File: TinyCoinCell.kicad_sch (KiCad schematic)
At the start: 35 parts, among them SW1 SW_Push, U1 nRF54L15-QFAA, X1 32MHz, X2 32.768kHz

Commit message: Updated with BOM
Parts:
- BT1: LCSC (none) -> C22417572
- C1, C2, C3, C4: LCSC (none) -> C2903664
- C10, C7: LCSC (none) -> C5377657
- C11, C14: LCSC (none) -> C723329
- C12: LCSC (none) -> C7393836
- C13: LCSC (none) -> C5142540
- C5: LCSC (none) -> C15525
- C6: LCSC (none) -> C18164554
- C8: LCSC (none) -> C18164580
- C9: LCSC (none) -> C18164556
- D1: LCSC (none) -> C52675989
- FB1: LCSC (none) -> C97850
- L1: LCSC (none) -> C295681
- L2: LCSC (none) -> C370148
- L3, L4, L5: LCSC (none) -> C52109755
- R1: LCSC (none) -> C102683
- R2: LCSC (none) -> C4125
- SW1: LCSC (none) -> C139797
- U1: LCSC (none) -> C42458750
- X1: LCSC (none) -> C2965582
- X2: LCSC (none) -> C2838163

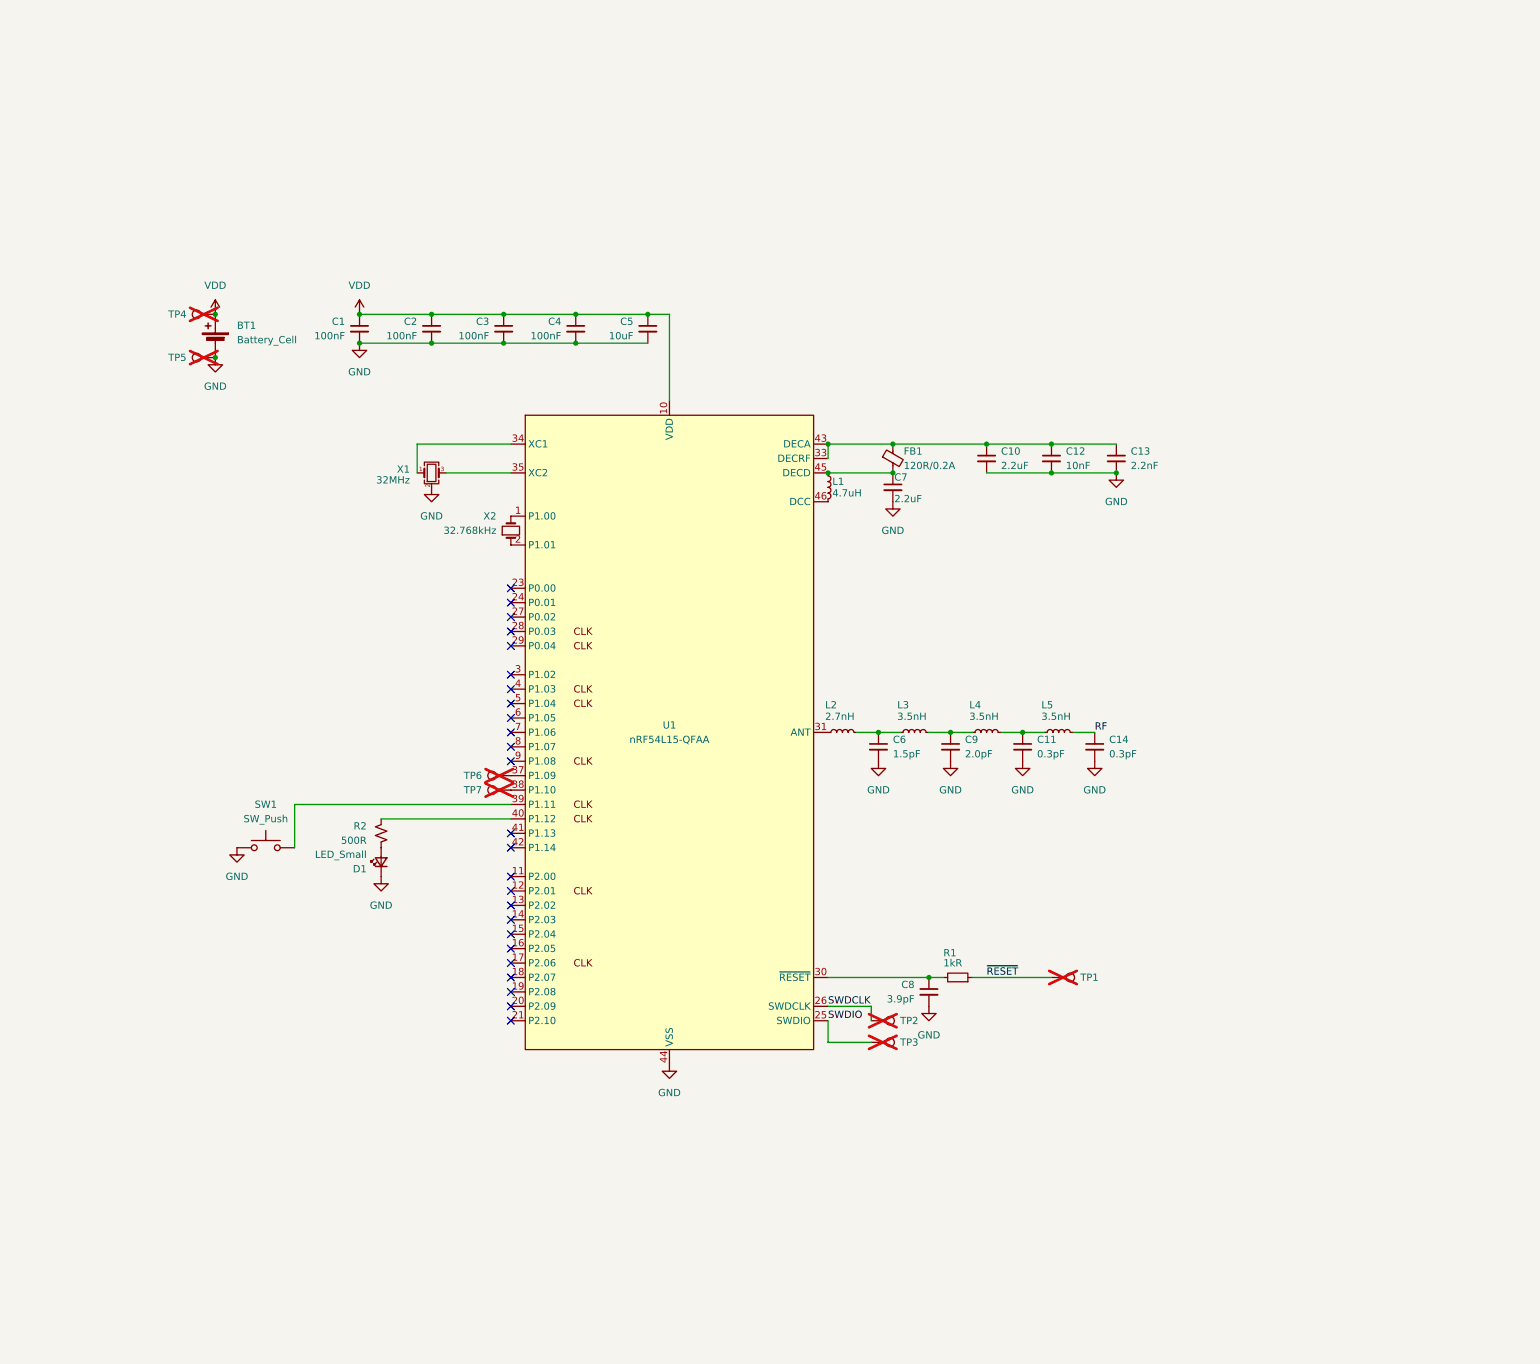
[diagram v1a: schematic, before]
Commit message: Updates for nPM2100
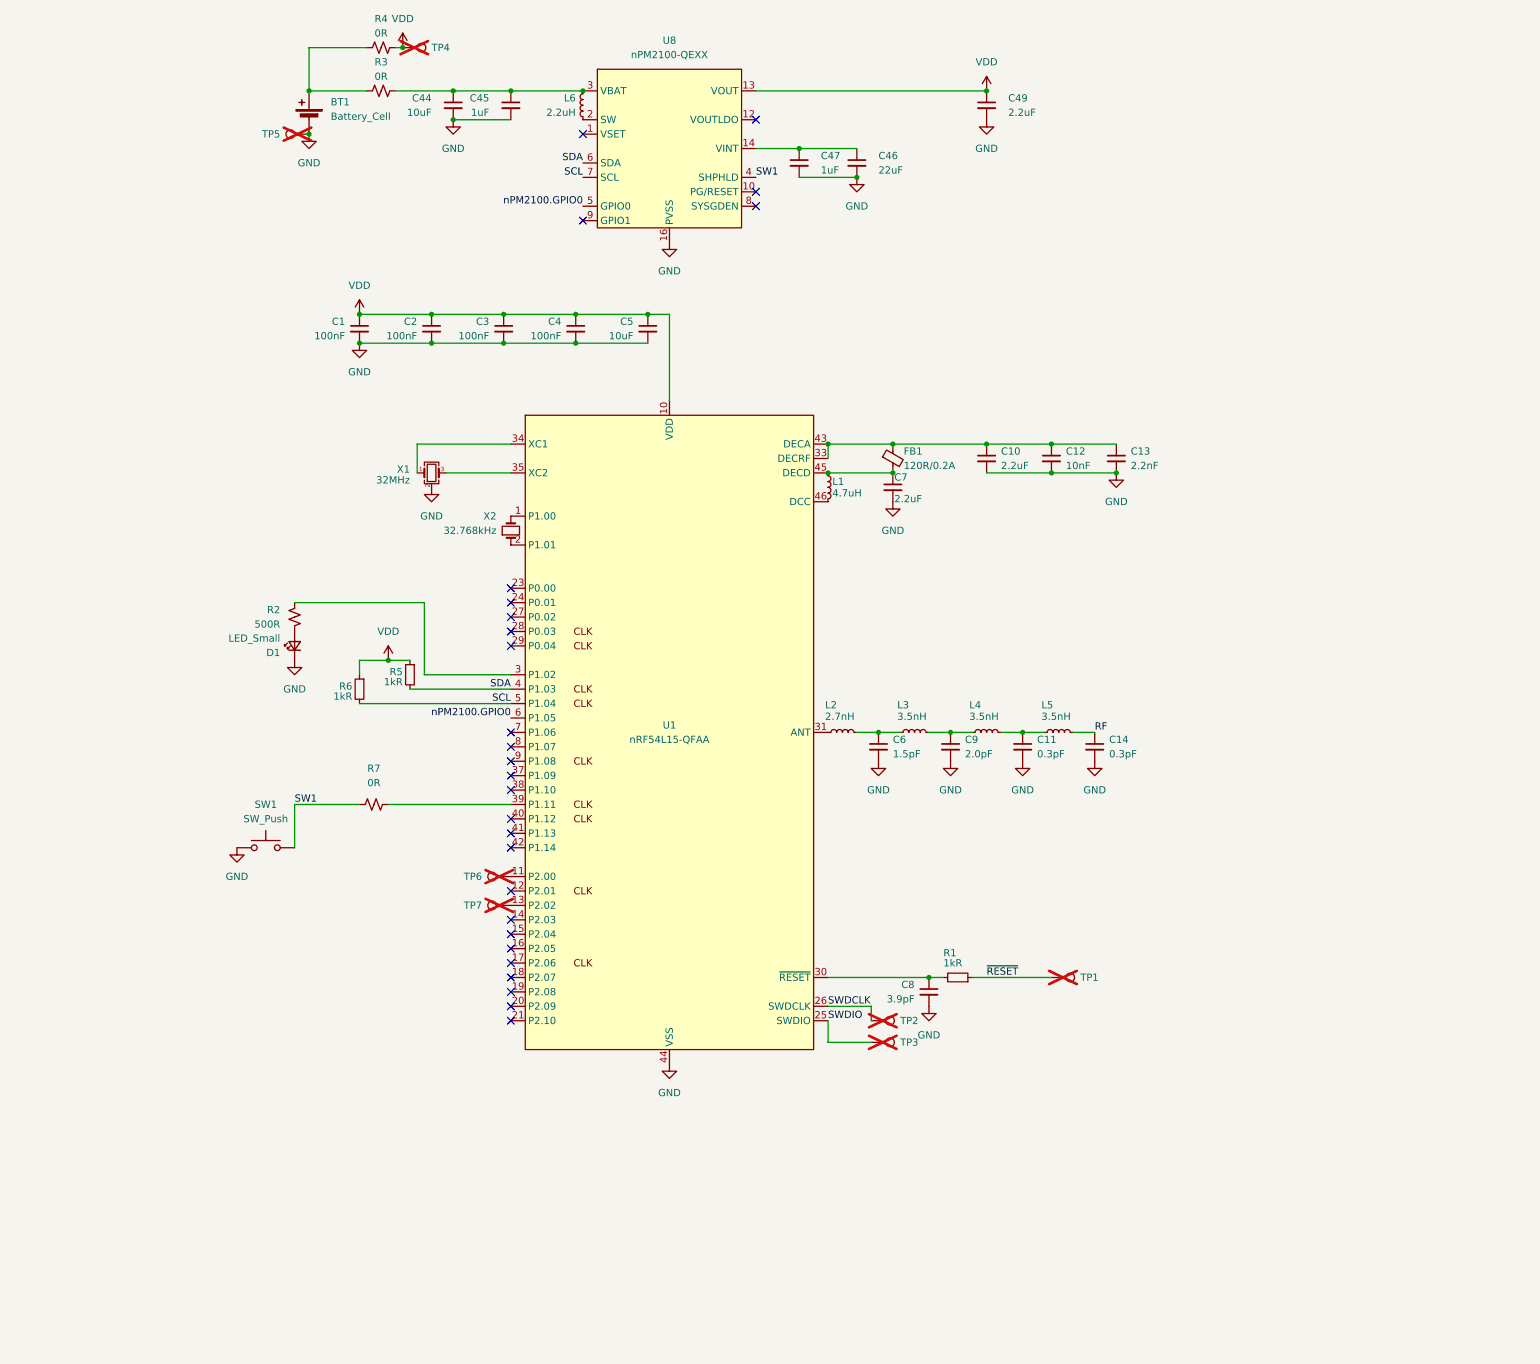
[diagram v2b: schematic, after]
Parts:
- added C44: 10uF, Capacitor_SMD:C_0402_1005Metric, symbol Device:C_Small
- added C45, C47: 1uF, Capacitor_SMD:C_0201_0603Metric, symbol Device:C_Small
- added C46: 22uF, Capacitor_SMD:C_0402_1005Metric, symbol Device:C_Small
- added C49: 2.2uF, Capacitor_SMD:C_0201_0603Metric, symbol Device:C_Small
- added L6: 2.2uH, Inductor_SMD:L_0603_1608Metric, symbol Device:L_Small
- added R3, R4, R7: 0R, Resistor_SMD:R_0402_1005Metric, symbol Device:R_Small_US
- added R5, R6: 1kR, passives:R_0201_0603Metric_L, symbol Device:R_Small
- added U8: nPM2100-QEXX, Package_DFN_QFN:UQFN-16-1EP_4x4mm_P0.65mm_EP2.6x2.6mm, symbol PCM_nordic-lib-kicad-npm:nPM2100-QEXX
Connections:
- net VDD: now also C49.1, R4.2, R5.1, R6.1, U8.13 (VOUT); no longer BT1.1 (+)
- net at TP7.1: now also U1.13 (P2.02); no longer U1.38 (P1.10)
- net at U1.39 (P1.11): now also R7.1; no longer SW1.1
- net at U1.11 (P2.00): now also TP6.1
- net at U1.3 (P1.02): now also R2.1
- net at U1.37 (P1.09): no longer TP6.1
- net SDA: now reaches U1.4 (P1.03)
- net SDA: now also R5.2, U8.6 (SDA)
- net at U1.40 (P1.12): no longer R2.1
- net SCL: now reaches U1.5 (P1.04)
- net SCL: now also R6.2, U8.7 (SCL)
- net nPM2100.GPIO0: now reaches U1.6 (P1.05)
- net nPM2100.GPIO0: now also U8.5 (GPIO0)
- net GND renamed AVSS2
- net AVSS2: now also C44.2, C45.2, C46.2, C47.2, C49.2, U8.11 (AVSS2), U8.16 (PVSS), U8.17 (EP)
- new net: C44.1, C45.1, L6.1, R3.2, U8.3 (VBAT)
- new net: C46.1, C47.1, U8.14 (VINT), U8.15 (VINT)
- new net: BT1.1 (+), R3.1, R4.1
- new net: L6.2, U8.2 (SW)
- new net SW1: R7.2, SW1.1, U8.4 (SHPHLD)
- no-connect marks 25 -> 27
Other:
- moved on the sheet: BT1, D1, R2, TP4, TP5, TP6, TP7

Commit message: Update for nPM2100, ADXL367
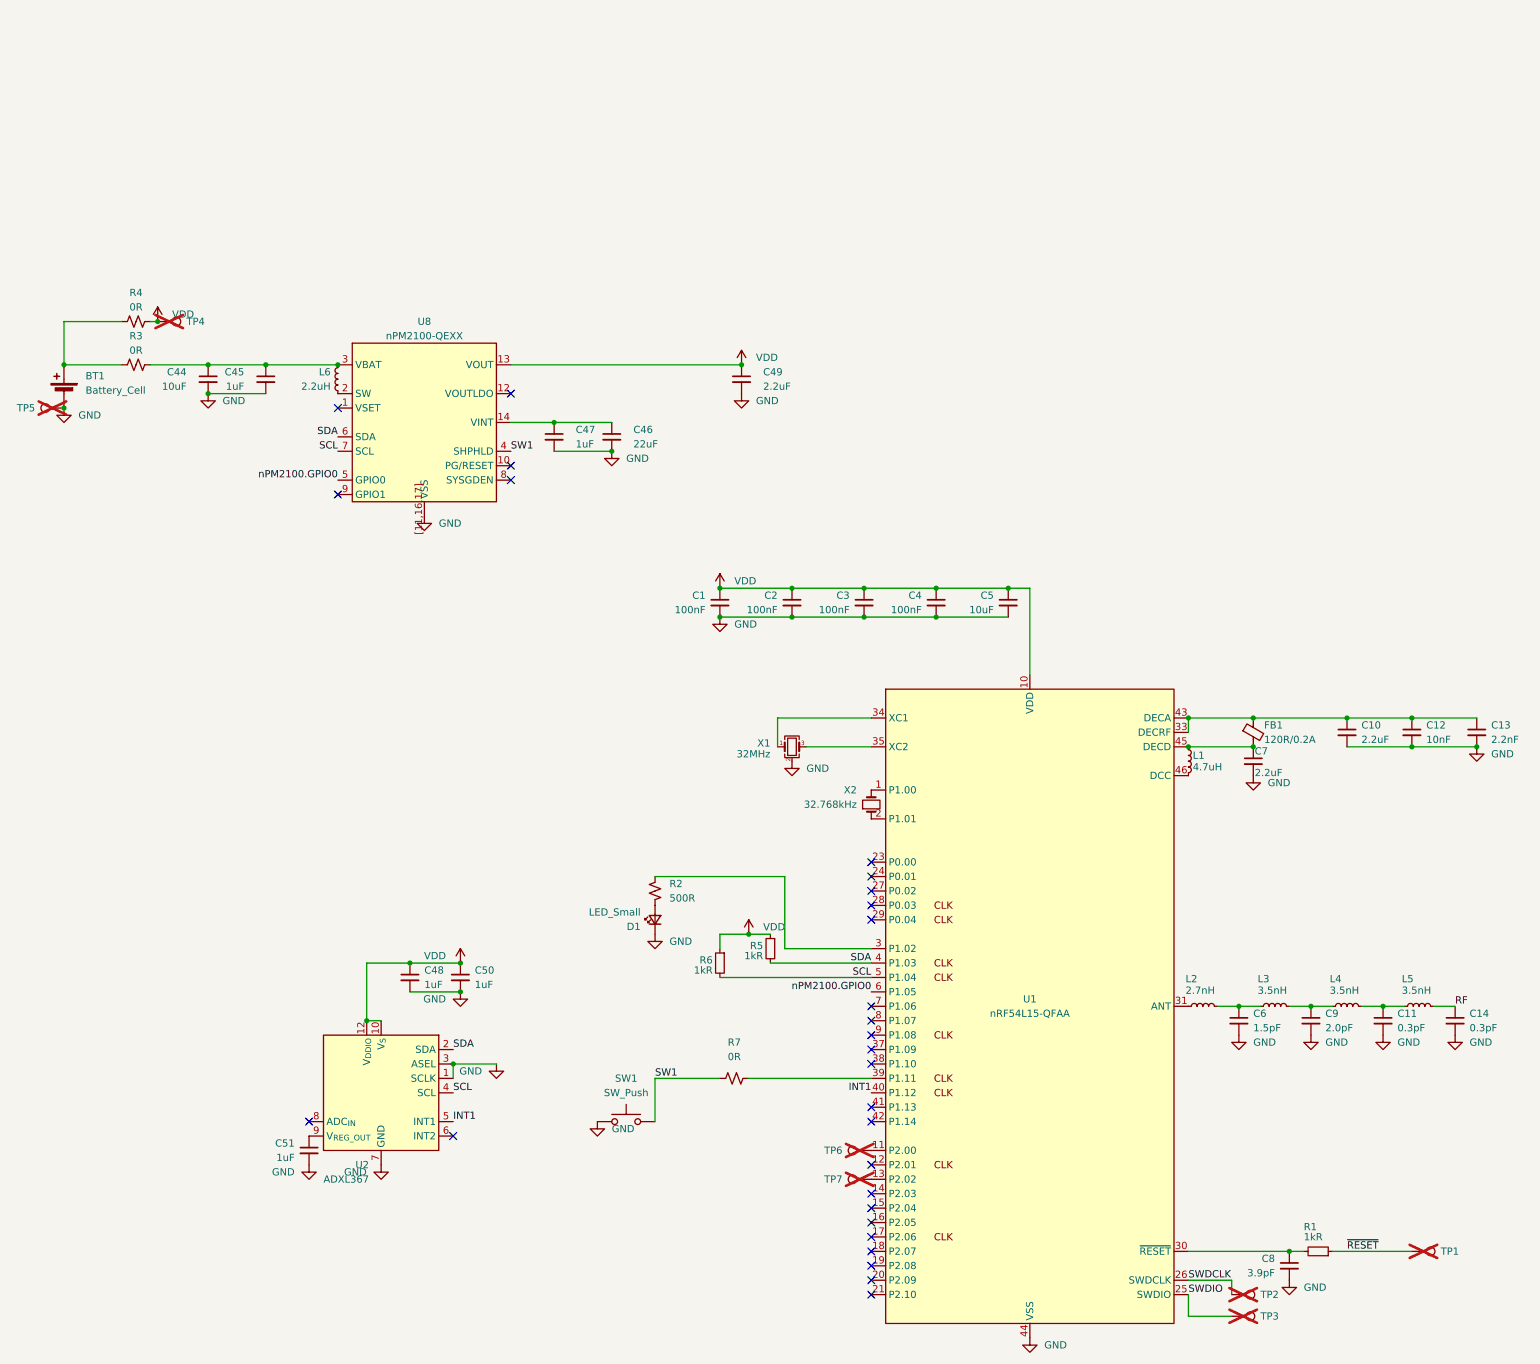
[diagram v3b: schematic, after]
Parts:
- added C48, C50, C51: 1uF, Capacitor_SMD:C_0201_0603Metric, symbol Device:C_Small
- added U2: ADXL367, TinyCoinCell:ADXL367_LGA-12_2.11x2.21mm_P0.5mm_LayoutBorder2x4y, symbol TinyCoinCell:ADXL367
- TP1, TP2, TP3, TP4, TP5, TP6, TP7: now in the parts list
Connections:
- net SCL: now also U2.4 (~{CS})
- net SDA: now also U2.2 (MOSI)
- net VDD: now also C48.1, C50.1, U2.10 (V_{S}), U2.12 (V_{DDIO})
- net INT1: now reaches U1.40 (P1.12)
- net INT1: now also U2.5 (INT1)
- net AVSS2 renamed GND
- net GND: now also U8.[11,16,17] (VSS), C48.2, C50.2, C51.2, U2.1 (SCLK), U2.11 (GND), U2.3 (MISO), U2.7 (GND); no longer U8.11 (AVSS2), U8.16 (PVSS), U8.17 (EP)
- new net: C51.1, U2.9 (V_{REG_OUT})
- no-connect marks 27 -> 28
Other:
- moved on the sheet: BT1, C44, C45, C46, C47, C49, L6, R3, R4, TP4, TP5, U8

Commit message: Updates for manufacturing
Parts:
- BT1: symbol Device:Battery_Cell -> amemb-Device:Battery_Cell_Jumper
- C14: value 0.3pF -> 1pF
- U1: footprint Package_DFN_QFN:QFN-48-1EP_6x6mm_P0.4mm_EP4.6x4.6mm -> Package_DFN_QFN:QFN-48-1EP_6x6mm_P0.4mm_EP4.6x4.6mm_ThermalVias
- U8: footprint Package_DFN_QFN:UQFN-16-1EP_4x4mm_P0.65mm_EP2.6x2.6mm -> Package_DFN_QFN:UQFN-16-1EP_4x4mm_P0.65mm_EP2.6x2.6mm_ThermalVias
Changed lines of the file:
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@@
 			)
 		)
-		(property "Value" "0.3pF"
+		(property "Value" "1pF"
 			(at 288.29 154.94 0)
 			(show_name no)
@@
 	)
 	(symbol
-		(lib_id "Device:Battery_Cell")
+		(lib_id "amemb-Device:Battery_Cell_Jumper")
 		(at 40.64 43.18 0)
 		(mirror y)
@@
 			)
 		)
-		(property "Footprint" "Package_DFN_QFN:QFN-48-1EP_6x6mm_P0.4mm_EP4.6x4.6mm"
+		(property "Footprint" "Package_DFN_QFN:QFN-48-1EP_6x6mm_P0.4mm_EP4.6x4.6mm_ThermalVias"
 			(at 210.82 224.79 0)
 			(hide yes)
@@
 			)
 		)
-		(property "Footprint" "Package_DFN_QFN:UQFN-16-1EP_4x4mm_P0.65mm_EP2.6x2.6mm"
+		(property "Footprint" "Package_DFN_QFN:UQFN-16-1EP_4x4mm_P0.65mm_EP2.6x2.6mm_ThermalVias"
 			(at 104.14 68.58 0)
 			(hide yes)
